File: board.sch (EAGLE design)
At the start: 86 parts, among them J1 AVR_SPI_PRG_6NS, U1 TPS2112A, U2 MAX1555, U3 USD-SOCKETNEW, U4 3.3V, U5 2.8V, U6 74HC595, Y1 8MHz, Y2 12.288MHz

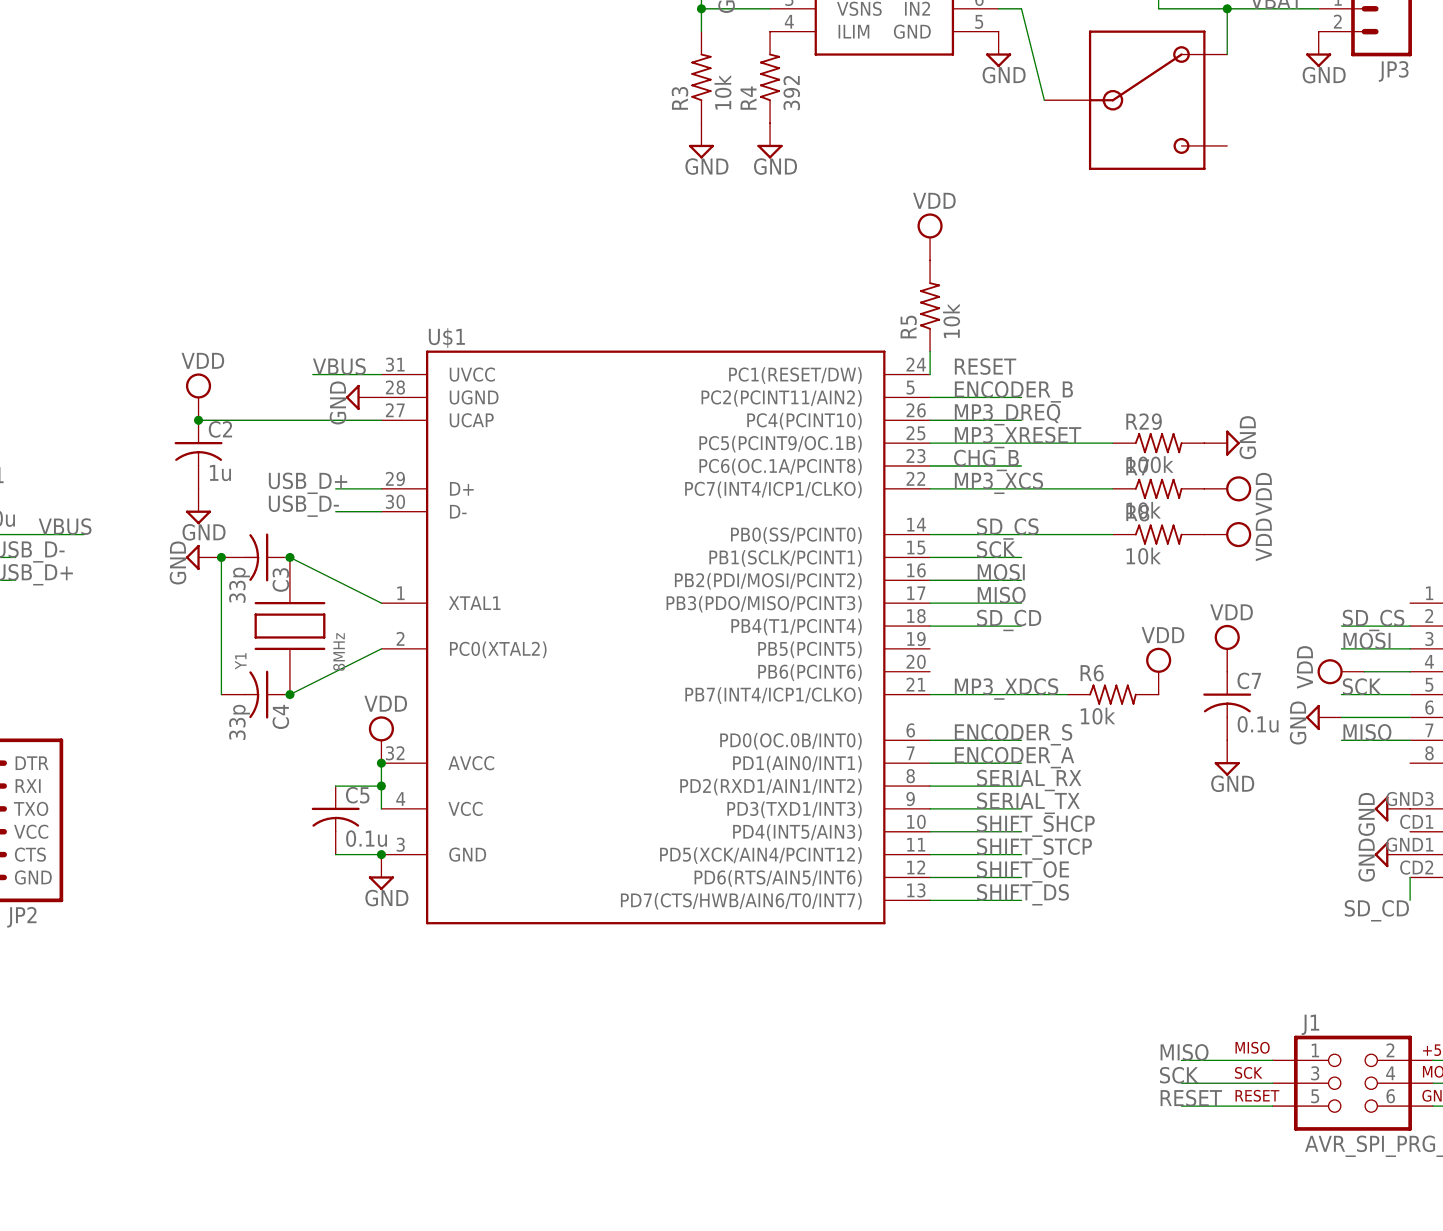
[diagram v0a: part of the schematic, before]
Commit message: Switching back to atmega32u4
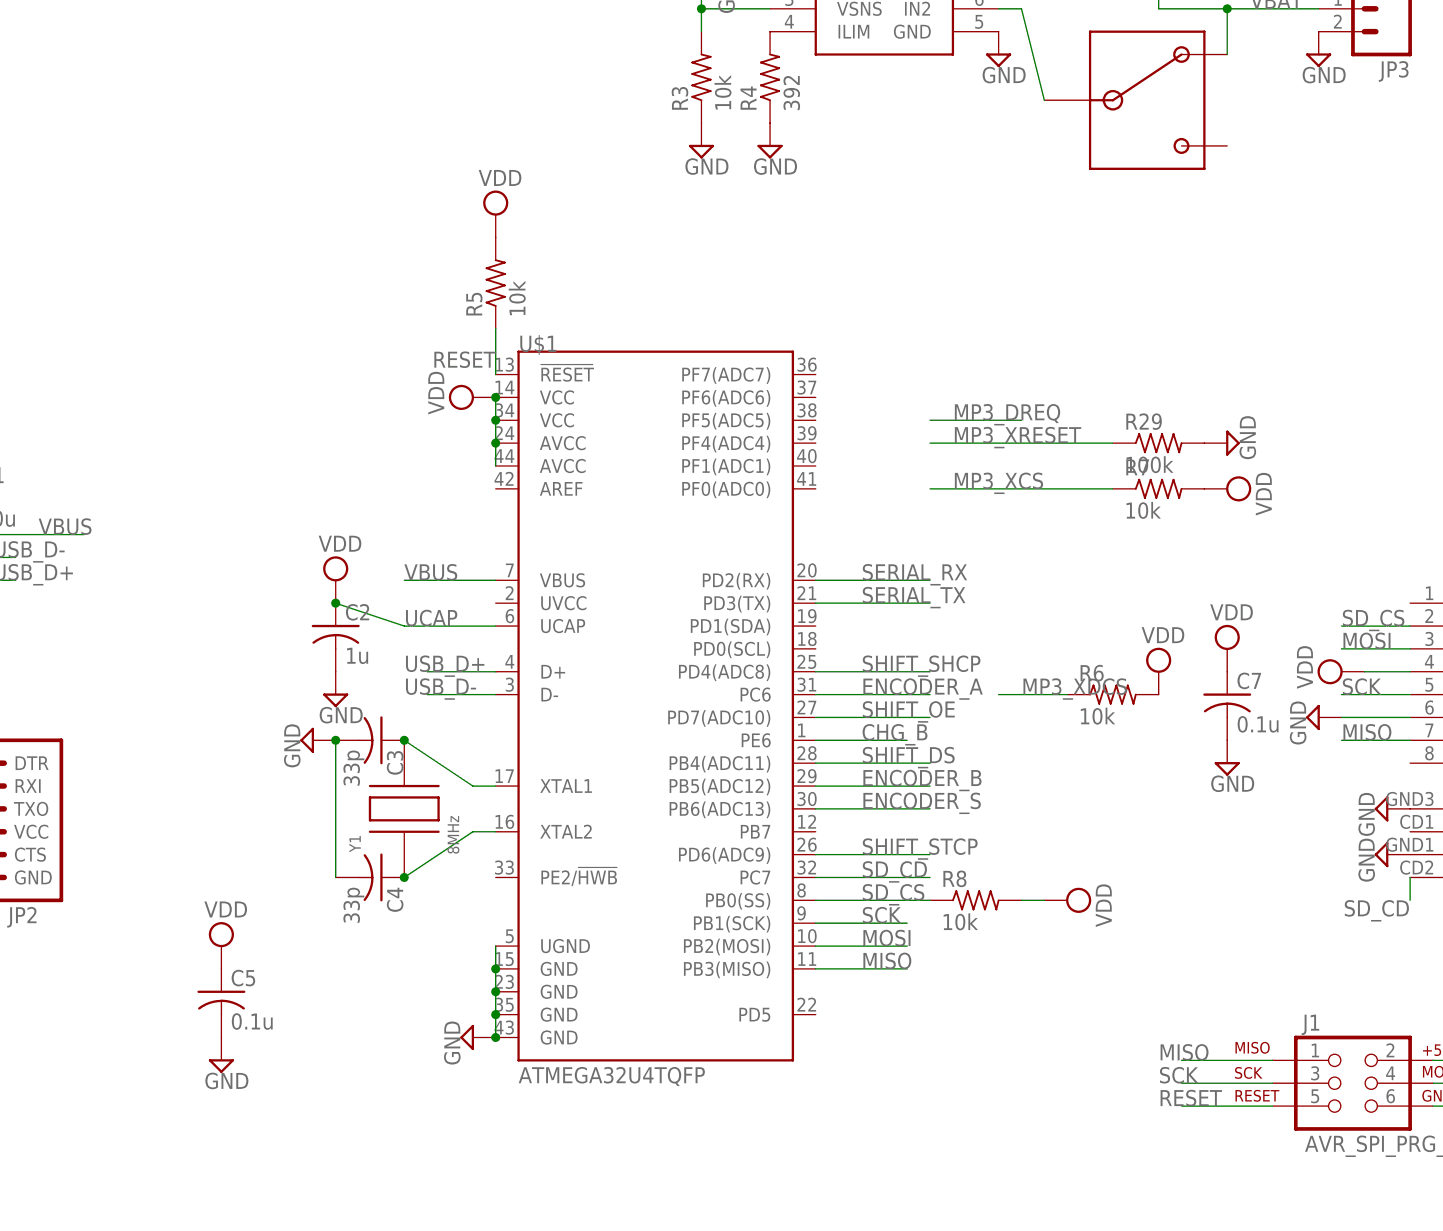
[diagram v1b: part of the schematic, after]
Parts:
- U$1: value ATMEGA32U2 -> ATMEGA32U4TQFP; device CEDT:ATMEGA32U2 -> SparkFun-DigitalIC:ATMEGA32U4TQFP
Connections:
- new net UCAP: C2.1, U$1.UCAP
- net CHG_B: now also U$1.PE6; no longer U$1.PC6(OC.1A/PCINT8)
- net ENCODER_A: now also U$1.PC6; no longer U$1.PD1(AIN0/INT1)
- net ENCODER_B: now also U$1.PB5(ADC12); no longer U$1.PC2(PCINT11/AIN2)
- net ENCODER_S: now also U$1.PB6(ADC13); no longer U$1.PD0(OC.0B/INT0)
- net GND: now also U$1.GND@15, U$1.GND@23, U$1.GND@35, U$1.GND@43; no longer U$1.GND
- net MISO: now also U$1.PB3(MISO); no longer U$1.PB3(PDO/MISO/PCINT3)
- net MOSI: now also U$1.PB2(MOSI); no longer U$1.PB2(PDI/MOSI/PCINT2)
- net MP3_DREQ: no longer U$1.PC4(PCINT10)
- net MP3_XCS: no longer U$1.PC7(INT4/ICP1/CLKO)
- net MP3_XDCS: no longer U$1.PB7(INT4/ICP1/CLKO)
- net MP3_XRESET: no longer U$1.PC5(PCINT9/OC.1B)
- net N$14: now also U$1.XTAL2; no longer U$1.PC0(XTAL2)
- net RESET: now also U$1.!RESET; no longer U$1.PC1(RESET/DW)
- net SCK: now also U$1.PB1(SCK); no longer U$1.PB1(SCLK/PCINT1)
- net SD_CD: now also U$1.PC7; no longer U$1.PB4(T1/PCINT4)
- net SD_CS: now also U$1.PB0(SS); no longer U$1.PB0(SS/PCINT0)
- net SERIAL_RX: now also U$1.PD2(RX); no longer U$1.PD2(RXD1/AIN1/INT2)
- net SERIAL_TX: now also U$1.PD3(TX); no longer U$1.PD3(TXD1/INT3)
- net SHIFT_DS: now also U$1.PB4(ADC11); no longer U$1.PD7(CTS/HWB/AIN6/T0/INT7)
- net SHIFT_OE: now also U$1.PD7(ADC10); no longer U$1.PD6(RTS/AIN5/INT6)
- net SHIFT_SHCP: now also U$1.PD4(ADC8); no longer U$1.PD4(INT5/AIN3)
- net SHIFT_STCP: now also U$1.PD6(ADC9); no longer U$1.PD5(XCK/AIN4/PCINT12)
- net VBUS: now also U$1.VBUS; no longer U$1.UVCC
- net VDD: now also U$1.AVCC@24, U$1.AVCC@44, U$1.VCC@14, U$1.VCC@34; no longer C2.1, U$1.AVCC, U$1.UCAP, U$1.VCC
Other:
- moved on the sheet: C2, C3, C4, C5, R5, R8, Y1

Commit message: Rough connections are made.
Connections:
- net MP3_DREQ: now also U$1.PF5(ADC5)
- net MP3_XCS: now also U$1.PF1(ADC1)
- net MP3_XDCS: now also U$1.PF0(ADC0)
- net MP3_XRESET: now also U$1.PF4(ADC4)
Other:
- moved on the sheet: R29, R6, R7
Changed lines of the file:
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@@
 <instance part="R13" gate="G$1" x="187.96" y="27.94" rot="R90"/>
 <instance part="SUPPLY10" gate="GND" x="180.34" y="20.32"/>
-<instance part="R7" gate="G$1" x="104.14" y="88.9"/>
+<instance part="R7" gate="G$1" x="93.98" y="91.44"/>
 <instance part="R8" gate="G$1" x="83.82" y="43.18"/>
-<instance part="R6" gate="G$1" x="99.06" y="66.04"/>
-<instance part="SUPPLY14" gate="G$1" x="104.14" y="68.58"/>
-<instance part="SUPPLY19" gate="G$1" x="111.76" y="88.9" rot="R270"/>
+<instance part="R6" gate="G$1" x="93.98" y="88.9"/>
+<instance part="SUPPLY14" gate="G$1" x="101.6" y="88.9" rot="R270"/>
+<instance part="SUPPLY19" gate="G$1" x="101.6" y="91.44" rot="R270"/>
 <instance part="SUPPLY52" gate="G$1" x="93.98" y="43.18" rot="R270"/>
-<instance part="R29" gate="G$1" x="104.14" y="93.98"/>
-<instance part="SUPPLY34" gate="GND" x="111.76" y="93.98" rot="R90"/>
+<instance part="R29" gate="G$1" x="93.98" y="93.98"/>
+<instance part="SUPPLY34" gate="GND" x="101.6" y="93.98" rot="R90"/>
 <instance part="U$1" gate="G$1" x="48.26" y="66.04"/>
 <instance part="SUPPLY53" gate="G$1" x="27.94" y="99.06" rot="R90"/>
@@
 <net name="MP3_XCS" class="0">
 <segment>
-<label x="81.28" y="88.9" size="1.778" layer="95"/>
+<label x="71.12" y="91.44" size="1.778" layer="95"/>
 <pinref part="R7" gate="G$1" pin="1"/>
-<wire x1="99.06" y1="88.9" x2="78.74" y2="88.9" width="0.1524" layer="91"/>
+<wire x1="88.9" y1="91.44" x2="66.04" y2="91.44" width="0.1524" layer="91"/>
+<pinref part="U$1" gate="G$1" pin="PF1(ADC1)"/>
 </segment>
 <segment>
@@
 </segment>
 <segment>
-<wire x1="86.36" y1="66.04" x2="93.98" y2="66.04" width="0.1524" layer="91"/>
-<label x="88.9" y="66.04" size="1.778" layer="95"/>
+<wire x1="66.04" y1="88.9" x2="88.9" y2="88.9" width="0.1524" layer="91"/>
+<label x="71.12" y="88.9" size="1.778" layer="95"/>
 <pinref part="R6" gate="G$1" pin="1"/>
+<pinref part="U$1" gate="G$1" pin="PF0(ADC0)"/>
 </segment>
 </net>
@@
 </segment>
 <segment>
-<wire x1="78.74" y1="96.52" x2="88.9" y2="96.52" width="0.1524" layer="91"/>
-<label x="81.28" y="96.52" size="1.778" layer="95"/>
+<label x="71.12" y="96.52" size="1.778" layer="95"/>
+<pinref part="U$1" gate="G$1" pin="PF5(ADC5)"/>
+<wire x1="88.9" y1="96.52" x2="66.04" y2="96.52" width="0.1524" layer="91"/>
 </segment>
 </net>
@@
 </segment>
 <segment>
-<label x="81.28" y="93.98" size="1.778" layer="95"/>
-<wire x1="78.74" y1="93.98" x2="99.06" y2="93.98" width="0.1524" layer="91"/>
+<label x="71.12" y="93.98" size="1.778" layer="95"/>
+<wire x1="66.04" y1="93.98" x2="88.9" y2="93.98" width="0.1524" layer="91"/>
 <pinref part="R29" gate="G$1" pin="1"/>
-</segment>
-</net>
+<pinref part="U$1" gate="G$1" pin="PF4(ADC4)"/>
+</segment>
+</net>

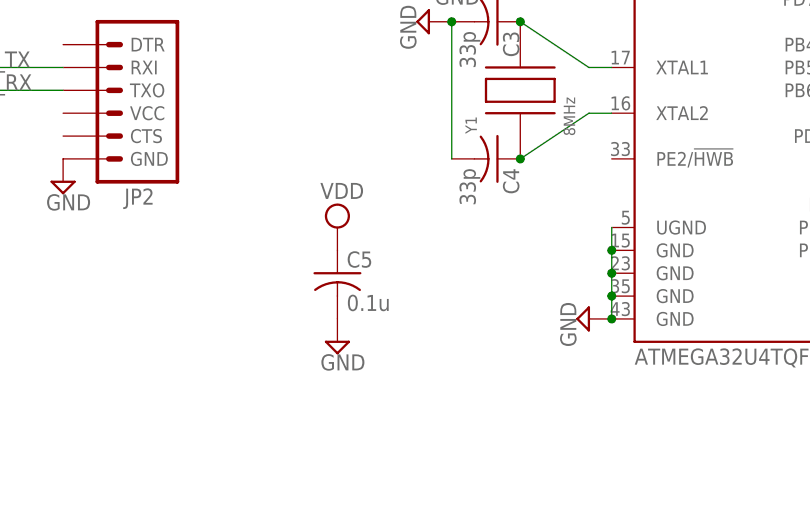
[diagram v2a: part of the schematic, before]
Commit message: More connections
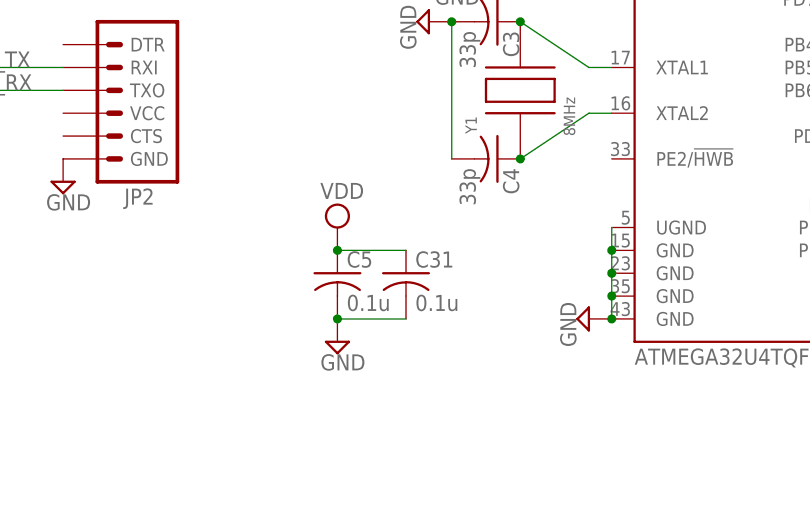
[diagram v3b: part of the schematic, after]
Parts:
- added C31: 0.1u, rcl:C-USC0603K
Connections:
- net GND: now also C31.2
- net VDD: now also C31.1
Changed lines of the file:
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@@
 <part name="U$1" library="SparkFun-DigitalIC" deviceset="ATMEGA32U4" device="TQFP"/>
 <part name="SUPPLY53" library="supply2" deviceset="VDD" device=""/>
+<part name="C31" library="rcl" deviceset="C-US" device="C0603K" value="0.1u"/>
 </parts>
 <sheets>
@@
 <instance part="U$1" gate="G$1" x="48.26" y="66.04"/>
 <instance part="SUPPLY53" gate="G$1" x="27.94" y="99.06" rot="R90"/>
+<instance part="C31" gate="G$1" x="7.62" y="33.02"/>
 </instances>
 <busses>
@@
 <pinref part="SUPPLY15" gate="G$1" pin="VDD"/>
 <pinref part="C5" gate="G$1" pin="1"/>
+<pinref part="C31" gate="G$1" pin="1"/>
+<wire x1="0" y1="35.56" x2="7.62" y2="35.56" width="0.1524" layer="91"/>
+<junction x="0" y="35.56"/>
 </segment>
 <segment>
@@
 <pinref part="SUPPLY41" gate="GND" pin="GND"/>
 <pinref part="C5" gate="G$1" pin="2"/>
-</segment>
-<segment>
+<pinref part="C31" gate="G$1" pin="2"/>
+<wire x1="7.62" y1="27.94" x2="0" y2="27.94" width="0.1524" layer="91"/>
+<junction x="0" y="27.94"/>
+</segment>
+<segment>
